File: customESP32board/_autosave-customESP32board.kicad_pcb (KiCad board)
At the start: 2 copper layers, 60 x 60 mm, 47 parts, among them J1 USB_B_Micro, J2 Conn_01x16_Pin, J3 Conn_01x16_Pin, Q1 S8050, Q2 S8050, Q3 BSS138, Q4 BSS138, Q5 BSS138, SW1 SW_Push, SW2 SW_Push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

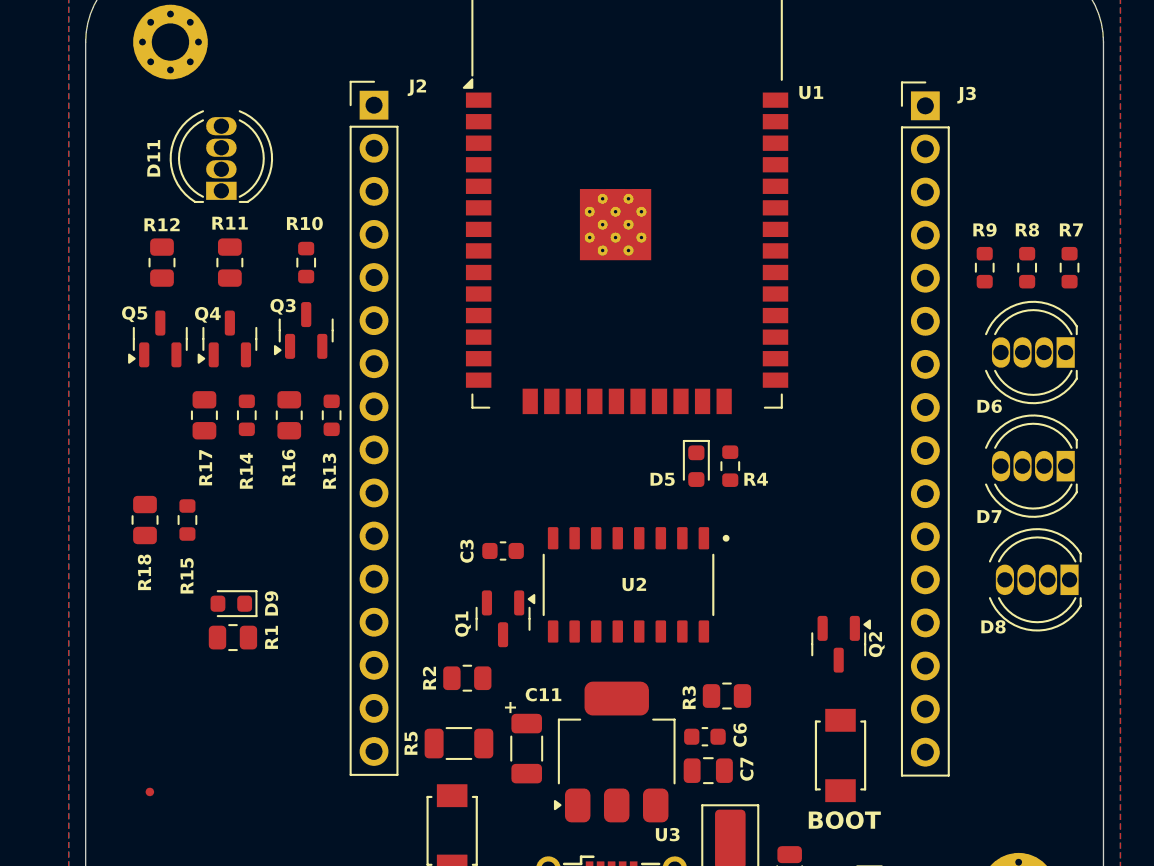
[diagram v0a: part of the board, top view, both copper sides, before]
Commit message: updated placement for metanoio pcb production rules
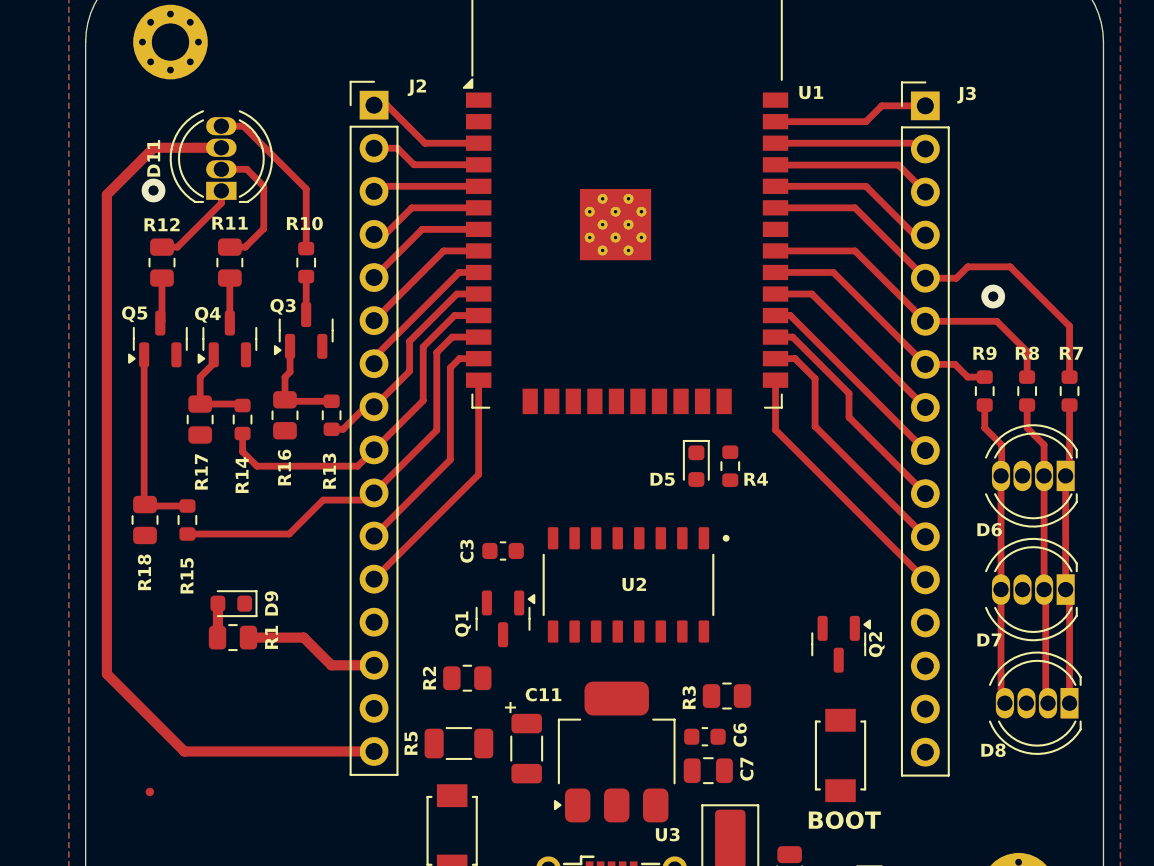
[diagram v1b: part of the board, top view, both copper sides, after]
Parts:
- moved D6 7.28 mm to (162.3, 104.1)
- moved D7 7.28 mm to (162.3, 110.8)
- moved R7 7.28 mm to (162.5, 99.1)
- moved R8 7.28 mm to (160.0, 99.1)
- moved R9 7.28 mm to (157.5, 99.1)
- moved D8 7.27 mm to (162.5, 117.5)
- moved R14 0.35 mm to (113.8, 100.8)
- moved R17 0.35 mm to (111.2, 100.8)
- moved R16 0.25 mm to (116.2, 100.5)
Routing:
- net +5V: track 0.00 -> 53.8 mm
- net ESP_IO27: track 0.00 -> 24.7 mm
- net ESP_IO21: track 0.00 -> 23.8 mm
- net ESP_IO26: track 0.00 -> 20.9 mm
- net ESP_IO19: track 0.00 -> 18.8 mm
- net RGB_RED: track 0.00 -> 18.1 mm
- net RGB_GREEN: track 0.00 -> 18.1 mm
- net RGB_BLUE: track 0.00 -> 17.8 mm
- net ESP_IO0: track 0.00 -> 15.4 mm
- net ESP_IO18: track 0.00 -> 14.9 mm
- net ESP_IO4: track 0.00 -> 14.8 mm
- net ESP_IO12: track 0.00 -> 14.3 mm
- net ESP_IO14: track 0.00 -> 13.7 mm
- net ESP_IO16: track 0.00 -> 13.5 mm
- net ESP_IO25: track 0.00 -> 13.0 mm
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
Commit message: updates check
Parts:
- moved R15 0.50 mm to (111.0, 106.7)
- moved R18 0.50 mm to (108.5, 106.7)
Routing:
- net ESP_IO27: track 24.7 -> 24.2 mm
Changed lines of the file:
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@@
 	(footprint "Resistor_SMD:R_0603_1608Metric"
 		(layer "F.Cu")
-		(at 110.5 106.675 -90)
+		(at 111 106.675 -90)
 		(descr "Resistor SMD 0603 (1608 Metric), square (rectangular) end terminal, IPC-7351 nominal, (Body size source: IPC-SM-782 page 72, https://www.pcb-3d.com/wordpress/wp-content/uploads/ipc-sm-782a_amendment_1_and_2.pdf), generated with kicad-footprint-generator")
 		(tags "resistor")
@@
 	(footprint "Resistor_SMD:R_0805_2012Metric"
 		(layer "F.Cu")
-		(at 108 106.675 -90)
+		(at 108.5 106.675 -90)
 		(descr "Resistor SMD 0805 (2012 Metric), square (rectangular) end terminal, IPC-7351 nominal, (Body size source: IPC-SM-782 page 72, https://www.pcb-3d.com/wordpress/wp-content/uploads/ipc-sm-782a_amendment_1_and_2.pdf), generated with kicad-footprint-generator")
 		(tags "resistor")
@@
 	)
 	(segment
-		(start 107.95 105.7125)
-		(end 108 105.7625)
+		(start 108.5 103.3)
+		(end 108.5 105.7625)
 		(width 0.4)
 		(layer "F.Cu")
@@
 	)
 	(segment
-		(start 110.5 105.85)
-		(end 108.0875 105.85)
+		(start 107.95 102.75)
+		(end 108.5 103.3)
 		(width 0.4)
 		(layer "F.Cu")
@@
 	)
 	(segment
-		(start 108.0875 105.85)
-		(end 108 105.7625)
+		(start 107.95 96.9375)
+		(end 107.95 102.75)
 		(width 0.4)
 		(layer "F.Cu")
@@
 	)
 	(segment
-		(start 107.95 96.9375)
-		(end 107.95 105.7125)
+		(start 108.5875 105.85)
+		(end 108.5 105.7625)
+		(width 0.4)
+		(layer "F.Cu")
+		(net 7)
+	)
+	(segment
+		(start 111 105.85)
+		(end 108.5875 105.85)
 		(width 0.4)
 		(layer "F.Cu")
@@
 	(segment
 		(start 116.5 107.5)
-		(end 110.5 107.5)
+		(end 111 107.5)
 		(width 0.4)
 		(layer "F.Cu")
@@
 	)
 	(segment
-		(start 121.08 105.5)
-		(end 118.5 105.5)
+		(start 125.199 96.801)
+		(end 126.1075 95.8925)
 		(width 0.4)
 		(layer "F.Cu")
@@
 	)
 	(segment
-		(start 125.199 96.801)
-		(end 126.1075 95.8925)
+		(start 121.08 105.5)
+		(end 118.5 105.5)
 		(width 0.4)
 		(layer "F.Cu")
@@
 	)
 	(segment
-		(start 105.75 115.75)
-		(end 105.75 87.5)
+		(start 108.52 84.73)
+		(end 112.5 84.73)
 		(width 0.6)
 		(layer "F.Cu")
@@
 	)
 	(segment
-		(start 121.5 120.32)
-		(end 110.32 120.32)
+		(start 110.32 120.32)
+		(end 106 116)
 		(width 0.6)
 		(layer "F.Cu")
@@
 	)
 	(segment
-		(start 105.75 87.5)
-		(end 108.52 84.73)
+		(start 121.5 120.32)
+		(end 110.32 120.32)
 		(width 0.6)
 		(layer "F.Cu")
@@
 	)
 	(segment
-		(start 110.32 120.32)
-		(end 105.75 115.75)
+		(start 106 87.25)
+		(end 108.52 84.73)
 		(width 0.6)
 		(layer "F.Cu")
@@
 	)
 	(segment
-		(start 108.52 84.73)
-		(end 112.5 84.73)
+		(start 106 116)
+		(end 106 87.25)
 		(width 0.6)
 		(layer "F.Cu")
